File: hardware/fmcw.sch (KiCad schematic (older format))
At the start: 28 parts, among them U2 LP5907-1.8, U35 LP5907MFX-3.3, U4 KT2520K, U5 NC7SVU04P5X, U6 NB3N551

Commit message: Changed components to official libs.
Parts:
- C12: value 1u -> 10n; footprint Capacitor_SMD:C_0603_1608Metric -> Capacitor_SMD:C_0402_1005Metric; MFN CL10B105MO8NNWC -> GRM155R71E103KA01D
- U2: value LP5907-1.8 -> LP5907MFX-1.2
- U4: footprint fmcw:KT2520K -> Oscillator:Oscillator_SMD_Kyocera_2520-6Pin_2.5x2.0mm; symbol fmcw-rescue:KT2520K-fmcw3-rescue -> Oscillator:KT2520K-T
- U5: symbol fmcw-rescue:NC7SVU04P5X -> 74xGxx:NC7SVU04P5X
- U6: footprint fmcw:DFN-8 -> Package_DFN_QFN:DFN-8-1EP_2x2mm_P0.5mm_EP0.8x1.2mm; symbol fmcw-rescue:NB3N551-fmcw3-rescue -> Interface:NB3N551MN
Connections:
- net GND: now also U6.9 (EP); no longer U6.EP
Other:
- moved on the sheet: C12, R13, R16, U6
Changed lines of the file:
@@
 ADF_TXDATA
 $Comp
-L fmcw-rescue:KT2520K-fmcw3-rescue U4
+L Oscillator:KT2520K-T U4
 U 1 1 59730F9D
-P 2100 6800
-F 0 "U4" H 2300 6550 60  0000 C CNN
-F 1 "KT2520K" H 2150 6950 60  0000 C CNN
-F 2 "fmcw:KT2520K" H 2100 6800 60  0001 C CNN
-F 3 "https://media.digikey.com/pdf/Data%20Sheets/AVX%20PDFs/KT2520K40000DAW18TAS_Spec.pdf" H 2100 6800 60  0001 C CNN
-F 4 "KT2520K40000DAW18TAS" H -200 0   50  0001 C CNN "MFN"
-	1    2100 6800
+P 2100 6850
+F 0 "U4" H 2000 7100 60  0000 R CNN
+F 1 "KT2520K" H 2550 7100 60  0000 R CNN
+F 2 "Oscillator:Oscillator_SMD_Kyocera_2520-6Pin_2.5x2.0mm" H 2100 6850 60  0001 C CNN
+F 3 "" H 2100 6850 60  0001 C CNN
+F 4 "KT2520K40000DAW18TAS" H -200 50  50  0001 C CNN "MFN"
+	1    2100 6850
 	1    0    0    -1
 $EndComp
@@
 L power:GND #PWR01
 U 1 1 597314F3
-P 1600 7050
-F 0 "#PWR01" H 1600 6800 50  0001 C CNN
-F 1 "GND" H 1600 6900 50  0000 C CNN
-F 2 "" H 1600 7050 60  0000 C CNN
-F 3 "" H 1600 7050 60  0000 C CNN
-	1    1600 7050
+P 2100 7200
+F 0 "#PWR01" H 2100 6950 50  0001 C CNN
+F 1 "GND" H 2100 7050 50  0000 C CNN
+F 2 "" H 2100 7200 60  0000 C CNN
+F 3 "" H 2100 7200 60  0000 C CNN
+	1    2100 7200
 	1    0    0    -1
 $EndComp
@@
 L Device:C C12
 U 1 1 597324ED
-P 1350 6700
-F 0 "C12" H 1375 6800 50  0000 L CNN
-F 1 "1u" H 1375 6600 50  0000 L CNN
-F 2 "Capacitor_SMD:C_0603_1608Metric" H 1388 6550 30  0001 C CNN
-F 3 "" H 1350 6700 60  0000 C CNN
-F 4 "CL10B105MO8NNWC" H 500 0   50  0001 C CNN "MFN"
-	1    1350 6700
+P 1650 6700
+F 0 "C12" H 1536 6746 50  0000 R CNN
+F 1 "10n" H 1536 6655 50  0000 R CNN
+F 2 "Capacitor_SMD:C_0402_1005Metric" H 1688 6550 30  0001 C CNN
+F 3 "" H 1650 6700 60  0000 C CNN
+F 4 "GRM155R71E103KA01D" H 800 0   50  0001 C CNN "MFN"
+	1    1650 6700
 	1    0    0    -1
 $EndComp
@@
 L power:GND #PWR02
 U 1 1 597328E7
-P 1350 6850
-F 0 "#PWR02" H 1350 6600 50  0001 C CNN
-F 1 "GND" H 1350 6700 50  0000 C CNN
-F 2 "" H 1350 6850 60  0000 C CNN
-F 3 "" H 1350 6850 60  0000 C CNN
-	1    1350 6850
-	1    0    0    -1
-$EndComp
-Text Label 1350 6550 0    60   ~ 0
+P 1650 6900
+F 0 "#PWR02" H 1650 6650 50  0001 C CNN
+F 1 "GND" H 1650 6750 50  0000 C CNN
+F 2 "" H 1650 6900 60  0000 C CNN
+F 3 "" H 1650 6900 60  0000 C CNN
+	1    1650 6900
+	1    0    0    -1
+$EndComp
+Text Label 1350 6500 0    60   ~ 0
 1V8_OSC
 Text Label 2900 5550 0    60   ~ 0
@@
 $EndComp
 $Comp
-L fmcw-rescue:NC7SVU04P5X U5
+L 74xGxx:NC7SVU04P5X U5
 U 1 1 5973922D
 P 3700 6850
@@
 $EndComp
 $Comp
-L fmcw-rescue:NB3N551-fmcw3-rescue U6
+L Interface:NB3N551MN U6
 U 1 1 5973DEB0
 P 5150 6800
 F 0 "U6" H 5350 6450 60  0000 C CNN
 F 1 "NB3N551" H 5450 7200 60  0000 C CNN
-F 2 "fmcw:DFN-8" H 5150 6800 60  0001 C CNN
-F 3 "http://www.onsemi.com/pub/Collateral/NB3N551-D.PDF" H 5150 6800 60  0001 C CNN
+F 2 "Package_DFN_QFN:DFN-8-1EP_2x2mm_P0.5mm_EP0.8x1.2mm" H 5150 6800 60  0001 C CNN
+F 3 "" H 5150 6800 60  0001 C CNN
 F 4 "NB3N551MNR4G" H 0   0   50  0001 C CNN "MFN"
 	1    5150 6800
@@
 U 1 1 5973E6F9
 P 4450 5300
-F 0 "FB1" V 4400 5200 50  0000 C CNN
-F 1 "BLM18PG181SH1D" V 4300 5300 50  0000 C CNN
+F 0 "FB1" V 4176 5300 50  0000 C CNN
+F 1 "BLM18PG181SH1D" V 4267 5300 50  0000 C CNN
 F 2 "Inductor_SMD:L_0603_1608Metric" H 4450 5300 60  0001 C CNN
 F 3 "https://www.murata.com/en-us/products/productdata/8796738650142/ENFA0003.pdf" H 4450 5300 60  0001 C CNN
@@
 L power:GND #PWR09
 U 1 1 597410B7
-P 5100 7400
-F 0 "#PWR09" H 5100 7150 50  0001 C CNN
-F 1 "GND" H 5100 7250 50  0000 C CNN
-F 2 "" H 5100 7400 60  0000 C CNN
-F 3 "" H 5100 7400 60  0000 C CNN
-	1    5100 7400
+P 5150 7300
+F 0 "#PWR09" H 5150 7050 50  0001 C CNN
+F 1 "GND" H 5150 7150 50  0000 C CNN
+F 2 "" H 5150 7300 60  0000 C CNN
+F 3 "" H 5150 7300 60  0000 C CNN
+	1    5150 7300
 	1    0    0    -1
 $EndComp
@@
 Wire Wire Line
 	8700 2800 8800 2800
-Wire Wire Line
-	1600 6850 1600 6950
-Connection ~ 1600 6950
-Wire Wire Line
-	1350 6550 1700 6550
 Wire Wire Line
 	1500 5650 1350 5650
@@
 Connection ~ 3700 6200
 Wire Wire Line
-	4500 6850 4650 6850
-Wire Wire Line
-	4500 6200 4500 6850
-Connection ~ 4500 6200
-Wire Wire Line
-	4350 6850 4350 6750
-Wire Wire Line
-	4350 6750 4650 6750
-Wire Wire Line
-	5100 7300 5100 7350
-Wire Wire Line
-	5200 7300 5200 7350
-Wire Wire Line
-	5200 7350 5100 7350
-Connection ~ 5100 7350
+	4700 6200 4700 6900
+Connection ~ 4700 6200
+Wire Wire Line
+	4350 6850 4350 6700
+Wire Wire Line
+	5150 7200 5150 7250
+Wire Wire Line
+	5250 7200 5250 7250
+Wire Wire Line
+	5250 7250 5150 7250
+Connection ~ 5150 7250
 $Comp
 L Device:R R13
 U 1 1 59741D92
-P 5950 6650
-F 0 "R13" V 5743 6650 50  0000 C CNN
-F 1 "33" V 5834 6650 50  0000 C CNN
-F 2 "Resistor_SMD:R_0402_1005Metric" V 5880 6650 30  0001 C CNN
-F 3 "" H 5950 6650 30  0000 C CNN
-F 4 "ERJ-2GEJ330X" H 0   150 50  0001 C CNN "MFN"
-	1    5950 6650
+P 5850 6600
+F 0 "R13" V 5643 6600 50  0000 C CNN
+F 1 "33" V 5734 6600 50  0000 C CNN
+F 2 "Resistor_SMD:R_0402_1005Metric" V 5780 6600 30  0001 C CNN
+F 3 "" H 5850 6600 30  0000 C CNN
+F 4 "ERJ-2GEJ330X" H -100 100 50  0001 C CNN "MFN"
+	1    5850 6600
 	0    1    1    0
 $EndComp
@@
 L Device:R R16
 U 1 1 5974223B
-P 5950 6850
-F 0 "R16" V 6065 6850 50  0000 C CNN
-F 1 "33" V 6156 6850 50  0000 C CNN
-F 2 "Resistor_SMD:R_0402_1005Metric" V 5880 6850 30  0001 C CNN
-F 3 "" H 5950 6850 30  0000 C CNN
-F 4 "ERJ-2GEJ330X" H 0   -150 50  0001 C CNN "MFN"
-	1    5950 6850
+P 5850 6800
+F 0 "R16" V 5965 6800 50  0000 C CNN
+F 1 "33" V 6056 6800 50  0000 C CNN
+F 2 "Resistor_SMD:R_0402_1005Metric" V 5780 6800 30  0001 C CNN
+F 3 "" H 5850 6800 30  0000 C CNN
+F 4 "ERJ-2GEJ330X" H -100 -200 50  0001 C CNN "MFN"
+	1    5850 6800
 	0    1    1    0
 $EndComp
 Wire Wire Line
-	6100 6650 6200 6650
-Wire Wire Line
-	6100 6850 6200 6850
-NoConn ~ 5650 6950
+	6000 6600 6100 6600
+Wire Wire Line
+	6000 6800 6100 6800
+NoConn ~ 5550 6900
 Wire Wire Line
 	10150 2050 10200 2050
 Text Label 10200 2050 0    60   ~ 0
 ADF_REF
-Text Label 6200 6850 0    60   ~ 0
+Text Label 6100 6800 0    60   ~ 0
 ADF_REF
-Text Label 6200 6650 0    60   ~ 0
+Text Label 6100 6600 0    60   ~ 0
 FPGA_REF
-Text Label 6200 6750 0    60   ~ 0
+Text Label 6100 6700 0    60   ~ 0
 ADC_REF
 Text Notes 800  5400 0    60   ~ 0
@@
 P 1800 5650
 F 0 "U2" H 1800 6039 60  0000 C CNN
-F 1 "LP5907-1.8" H 1800 5933 60  0000 C CNN
+F 1 "LP5907MFX-1.2" H 1800 5933 60  0000 C CNN
 F 2 "Package_TO_SOT_SMD:SOT-23-5" H 1800 5700 60  0001 C CNN
 F 3 "" H 1800 5700 60  0001 C CNN
@@
 3V0: 70 mA
 Wire Wire Line
-	1600 6950 1600 7050
-Wire Wire Line
 	1350 5550 1500 5550
 Wire Wire Line
@@
 	4800 5300 5150 5300
 Wire Wire Line
-	5150 6200 5150 6250
-Wire Wire Line
-	4500 6200 4700 6200
-Wire Wire Line
-	5100 7350 5100 7400
-Wire Wire Line
-	5650 6650 5800 6650
-Wire Wire Line
-	5650 6850 5800 6850
+	4700 6200 4450 6200
+Wire Wire Line
+	5150 7250 5150 7300
+Wire Wire Line
+	5550 6600 5700 6600
+Wire Wire Line
+	5550 6800 5700 6800
 Wire Wire Line
 	4600 5300 4800 5300
@@
 L power:PWR_FLAG #FLG0101
 U 1 1 5CE75A5A
-P 4700 6200
-F 0 "#FLG0101" H 4700 6275 50  0001 C CNN
-F 1 "PWR_FLAG" H 4700 6374 50  0000 C CNN
-F 2 "" H 4700 6200 50  0001 C CNN
-F 3 "~" H 4700 6200 50  0001 C CNN
-	1    4700 6200
-	1    0    0    -1
-$EndComp
-Connection ~ 4700 6200
-Wire Wire Line
-	4700 6200 5150 6200
+P 4450 6200
+F 0 "#FLG0101" H 4450 6275 50  0001 C CNN
+F 1 "PWR_FLAG" H 4450 6374 50  0000 C CNN
+F 2 "" H 4450 6200 50  0001 C CNN
+F 3 "~" H 4450 6200 50  0001 C CNN
+	1    4450 6200
+	1    0    0    -1
+$EndComp
 Wire Wire Line
 	1800 5950 1800 6000
@@
 Wire Wire Line
 	3300 6650 3300 6850
-Wire Wire Line
-	1700 6850 1600 6850
-Wire Wire Line
-	1700 6950 1600 6950
-Wire Wire Line
-	1700 6750 1700 6550
 $Comp
 L Device:R R3
@@
 Connection ~ 2700 6850
 Wire Wire Line
-	2700 6850 2550 6850
-Wire Wire Line
 	3800 6500 3700 6500
 Connection ~ 3700 6500
@@
 Wire Wire Line
 	4150 6500 4150 6600
-Wire Wire Line
-	3700 6200 4500 6200
 $Comp
 L Device:Ferrite_Bead FB15
@@
 	4800 5750 4800 5700
 Wire Wire Line
-	5650 6750 6200 6750
+	5550 6700 6100 6700
 $Comp
 L Regulator_Linear:LP5907MFX-3.3 U?
@@
 Wire Wire Line
 	2700 5550 2900 5550
+Wire Wire Line
+	2100 7200 2100 7150
+Wire Wire Line
+	2100 6500 2100 6550
+Wire Wire Line
+	1350 6500 1650 6500
+Wire Wire Line
+	1650 6900 1650 6850
+Wire Wire Line
+	1650 6550 1650 6500
+Connection ~ 1650 6500
+Wire Wire Line
+	1650 6500 2100 6500
+Wire Wire Line
+	2400 6850 2700 6850
+Wire Wire Line
+	5150 6200 5150 6400
+Wire Wire Line
+	4350 6700 4750 6700
+Wire Wire Line
+	4700 6900 4750 6900
+Wire Wire Line
+	4700 6200 5150 6200
+Connection ~ 4450 6200
+Wire Wire Line
+	3700 6200 4450 6200
 $EndSCHEMATC

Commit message: Finished design, began routing.
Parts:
- C7: renamed from C142; MFN CL21B106KQQNNNE -> (none)
- U1: renamed from U35; MFN (none) -> LP5907MFX-3.3/NOPB
- U2: value LP5907MFX-1.2 -> LP5907MFX-1.8
- U3: renamed from U4; value KT2520K -> KT2520K-T
- renumbered C16 to C10, C15 to C11, C145 to C12, C17 to C13, C140 to C2, C9 to C3, C12 to C4, C141 to C5, C144 to C6, C143 to C8, C13 to C9, FB15 to FB1, FB1 to FB2, H3 to H2, H2 to H3, R3 to R1, R8 to R2, R11 to R3, R13 to R4, R16 to R5, U5 to U4, U6 to U5
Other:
- moved on the sheet: C1, C2, C3, C5, C6, C7, C8, FB1, U1, U2

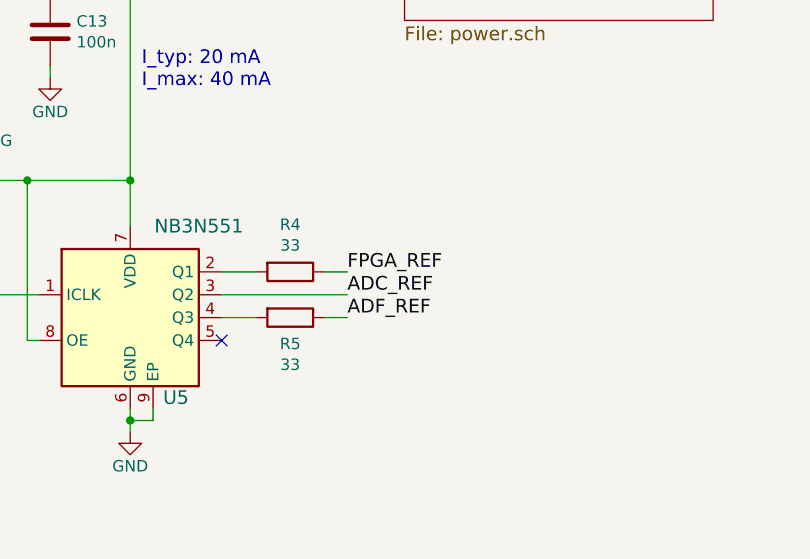
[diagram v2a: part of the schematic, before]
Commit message: Placed most major components.
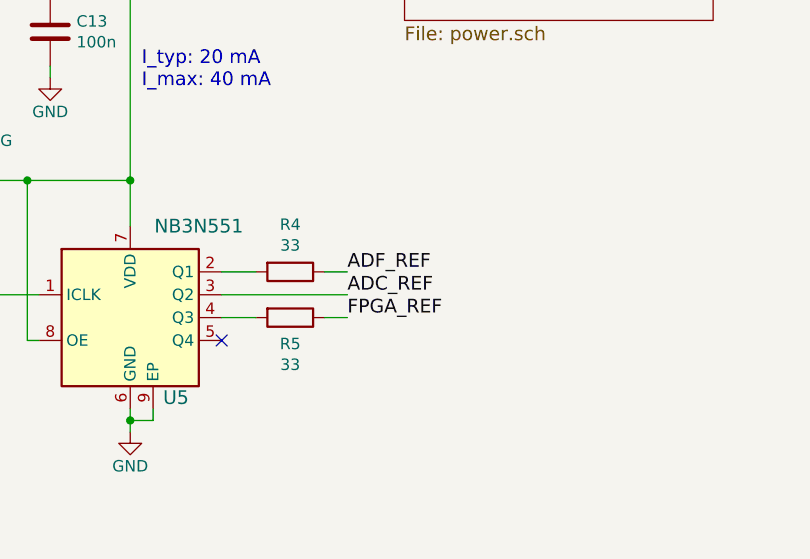
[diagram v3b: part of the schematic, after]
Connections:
- net ADF_REF: now also R4.1; no longer R5.1
- net FPGA_REF: now also R5.1; no longer R4.1
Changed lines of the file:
@@
 Text Label 10200 2050 0    60   ~ 0
 ADF_REF
+Text Label 6100 6600 0    60   ~ 0
+ADF_REF
 Text Label 6100 6800 0    60   ~ 0
-ADF_REF
-Text Label 6100 6600 0    60   ~ 0
 FPGA_REF
 Text Label 6100 6700 0    60   ~ 0

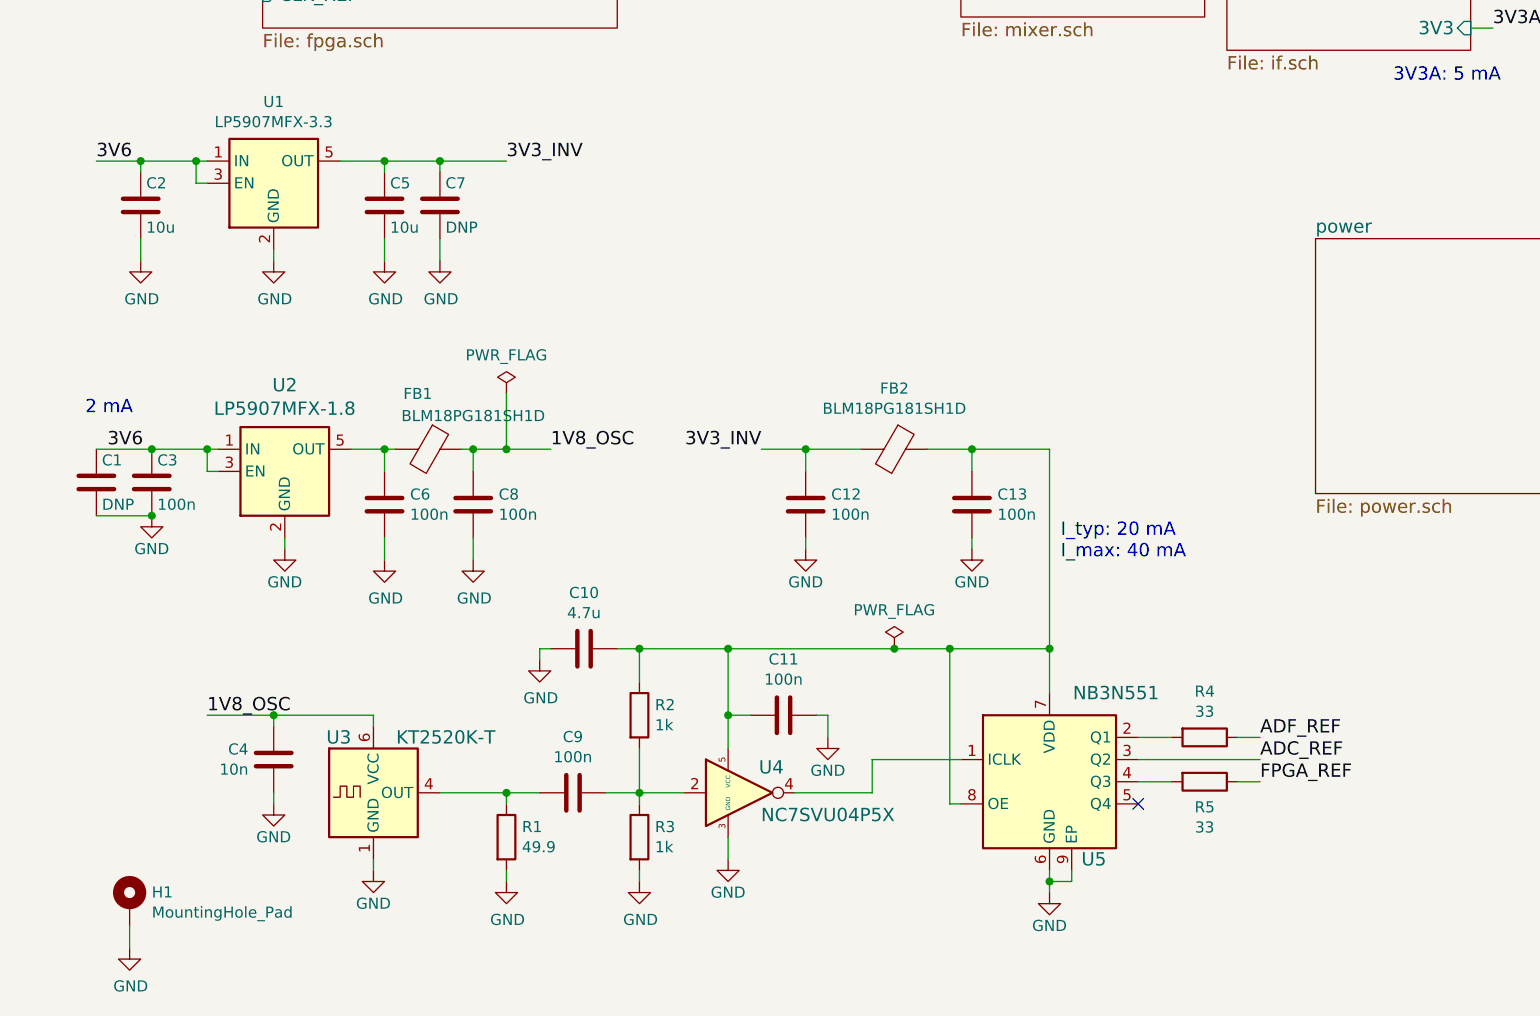
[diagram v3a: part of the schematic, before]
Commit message: Completed clock placement and routing.
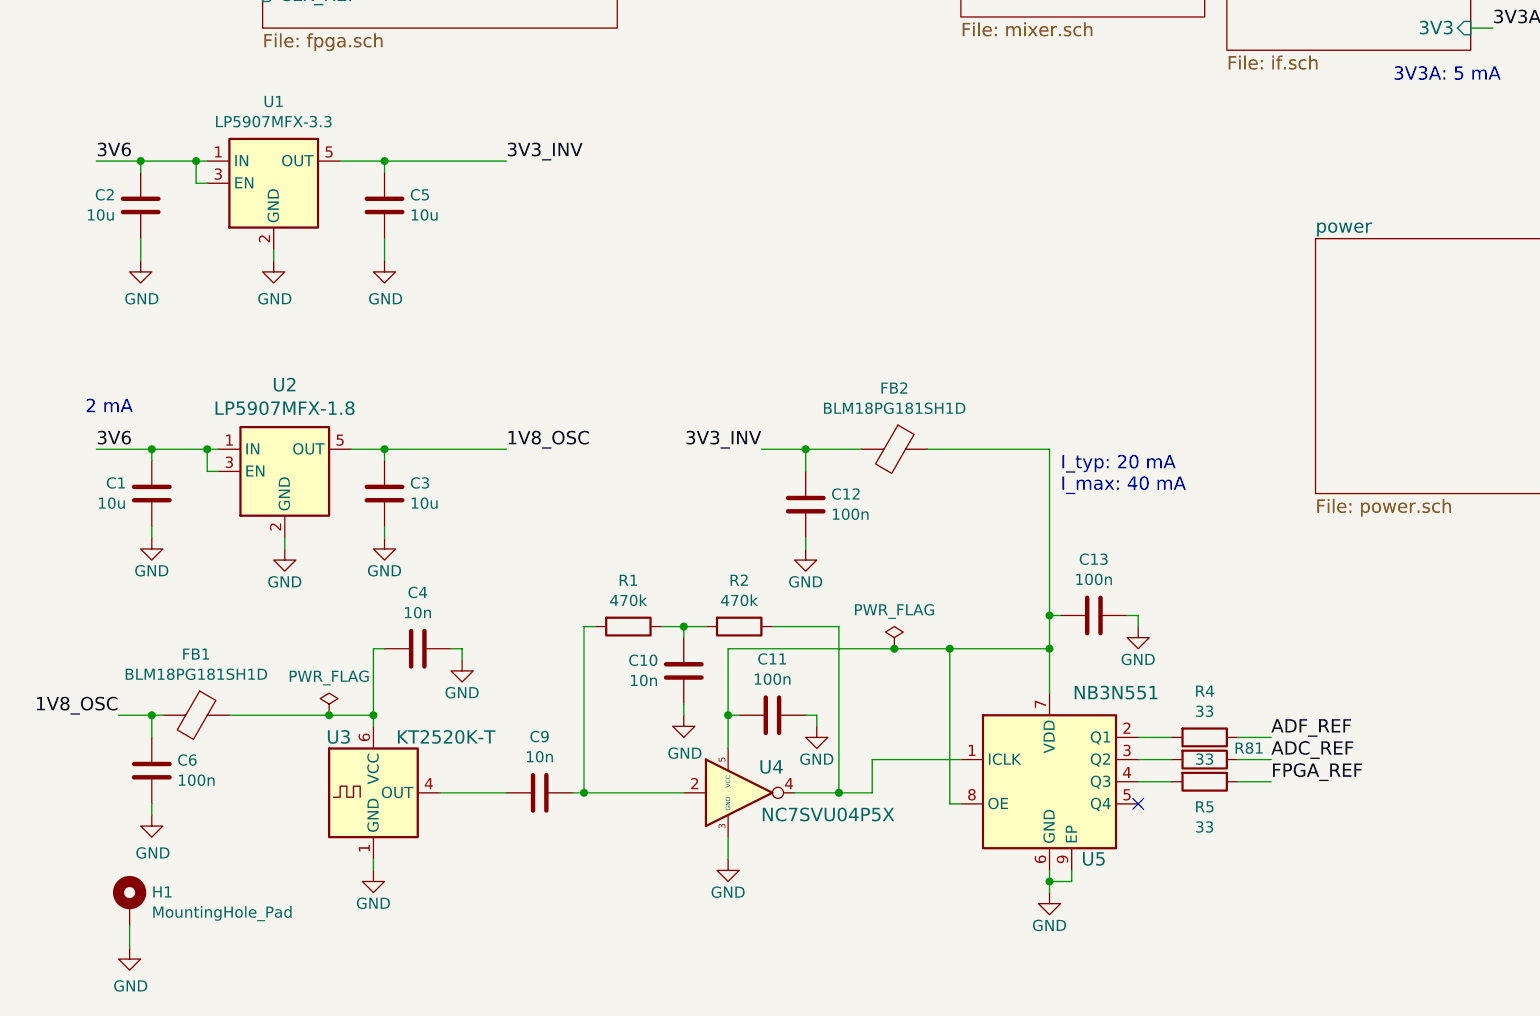
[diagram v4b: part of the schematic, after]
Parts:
- removed C7: DNP, Capacitor_SMD:C_0805_2012Metric, symbol Device:C
- removed C8: 100n, Capacitor_SMD:C_0402_1005Metric, symbol Device:C
- removed R3: 1k, Resistor_SMD:R_0402_1005Metric, symbol Device:R
- added R81: 33, Resistor_SMD:R_0402_1005Metric, symbol Device:R
- C1: value DNP -> 10u; MFN (none) -> CL21B106KQQNNNE
- C10: value 4.7u -> 10n; footprint Capacitor_SMD:C_0603_1608Metric -> Capacitor_SMD:C_0402_1005Metric; MFN CL10A475KA8NQNC -> GRM155R71E103KA01D
- C3: value 100n -> 10u; footprint Capacitor_SMD:C_0402_1005Metric -> Capacitor_SMD:C_0805_2012Metric; MFN CL05B104KO5NNNC -> CL21B106KQQNNNE
- C9: value 100n -> 10n; MFN CL05B104KO5NNNC -> GRM155R71E103KA01D
- R1: value 49.9 -> 470k; MFN ERJ-2RKF49R9X -> ERJ-2RKF4703X
- R2: value 1k -> 470k; MFN ERJ-2RKF1001X -> ERJ-2RKF4703X
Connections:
- net 1V8_OSC: now also C3.1, C6.1, FB1.2, U2.5 (OUT); no longer C4.1, FB1.1, U3.6 (VCC)
- net 3V6: no longer C3.1
- net ADC_REF: now also R81.1; no longer U5.3 (Q2)
- net GND: now also C10.1, C13.1, C4.1; no longer C10.2, C13.2, C4.2, R1.2
- net at C9.2, U3.4 (OUT): no longer R1.1
- net at C9.1, U4.2: now also R1.2; no longer R2.2
- net at U4.4, U5.1 (ICLK): now also R2.1
- net at C11.2, FB2.1, U4.5 (VCC)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: now also C13.2; no longer C10.1, C13.1, R2.1
- new net: C4.2, FB1.1, U3.6 (VCC)
- new net: R81.2, U5.3 (Q2)
- new net: C10.2, R1.1, R2.2
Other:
- moved on the sheet: C11, C13, C4, C6, FB1
